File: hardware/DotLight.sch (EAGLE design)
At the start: 19 parts, among them Q1 BSH103, Q2 BSH103

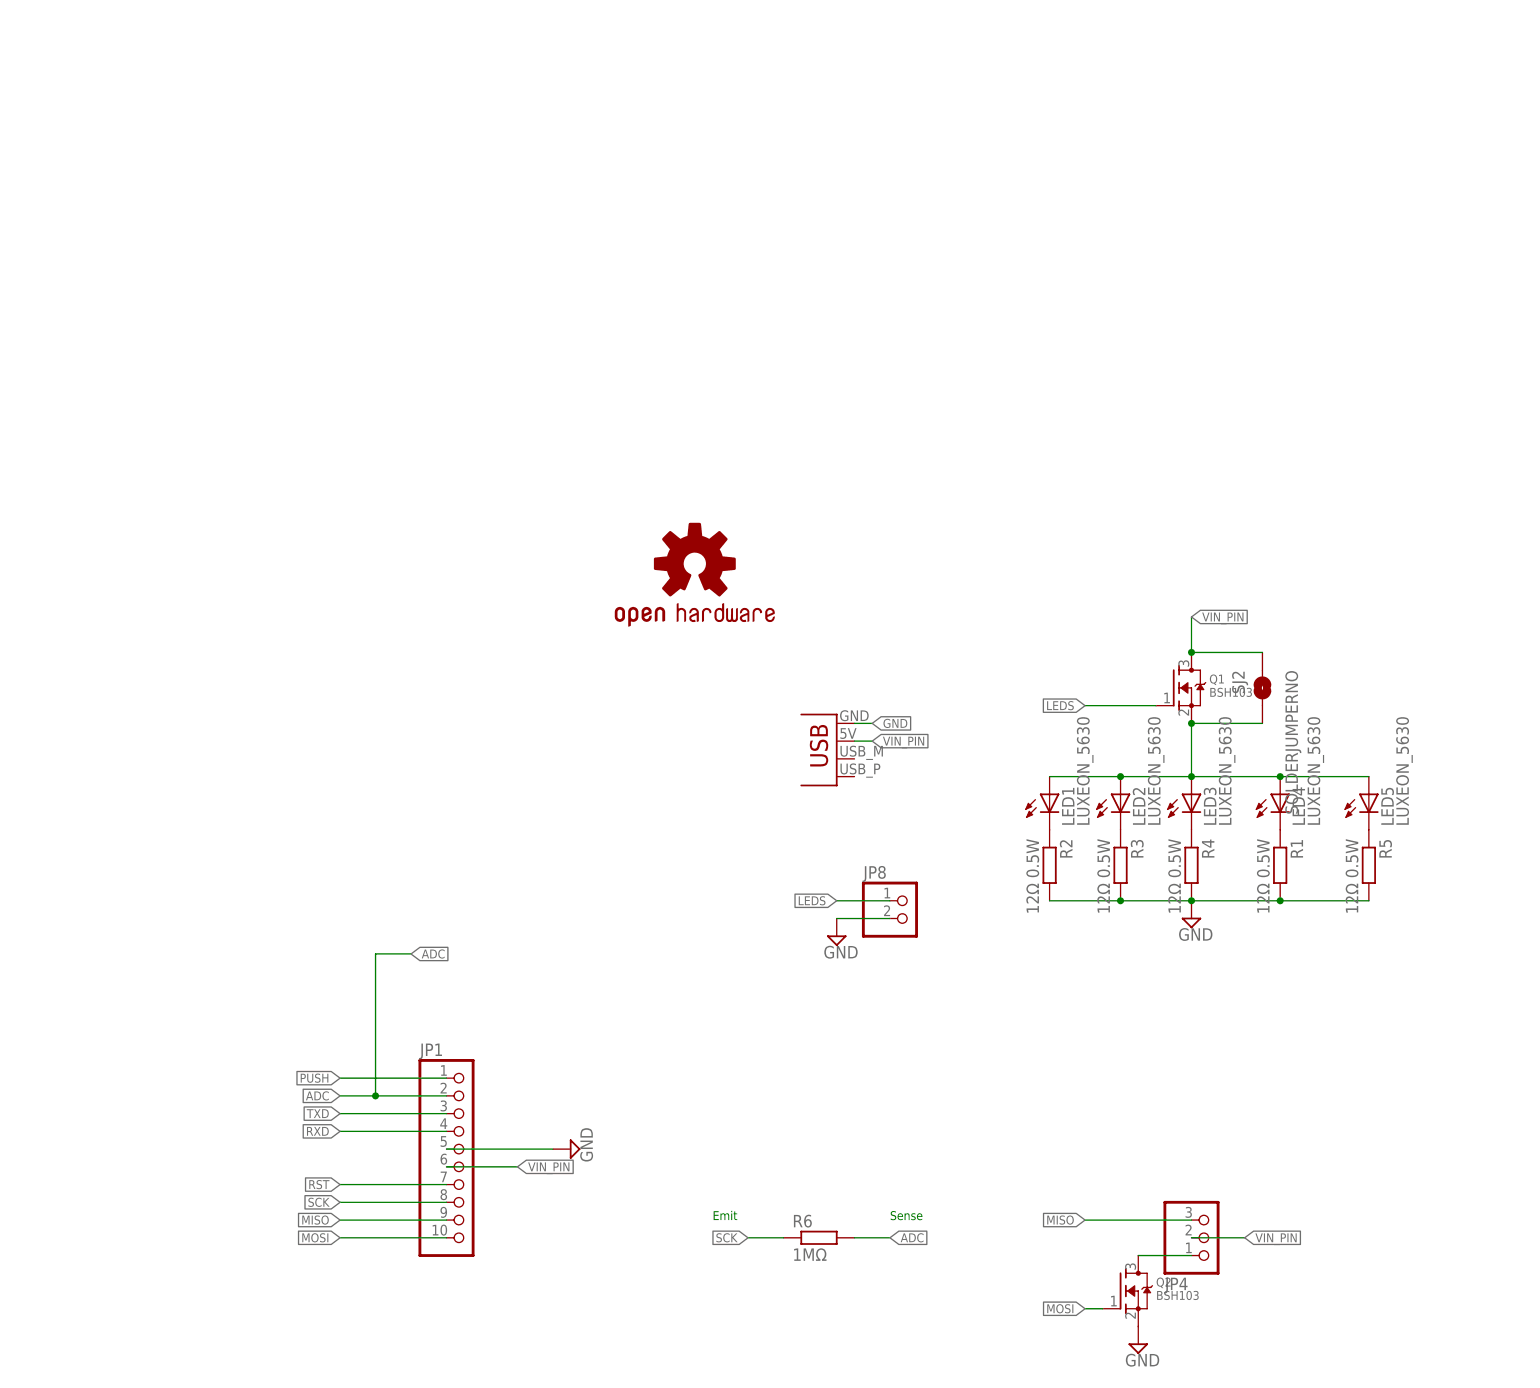
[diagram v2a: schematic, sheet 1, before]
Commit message: Add Attiny85 and usage logos
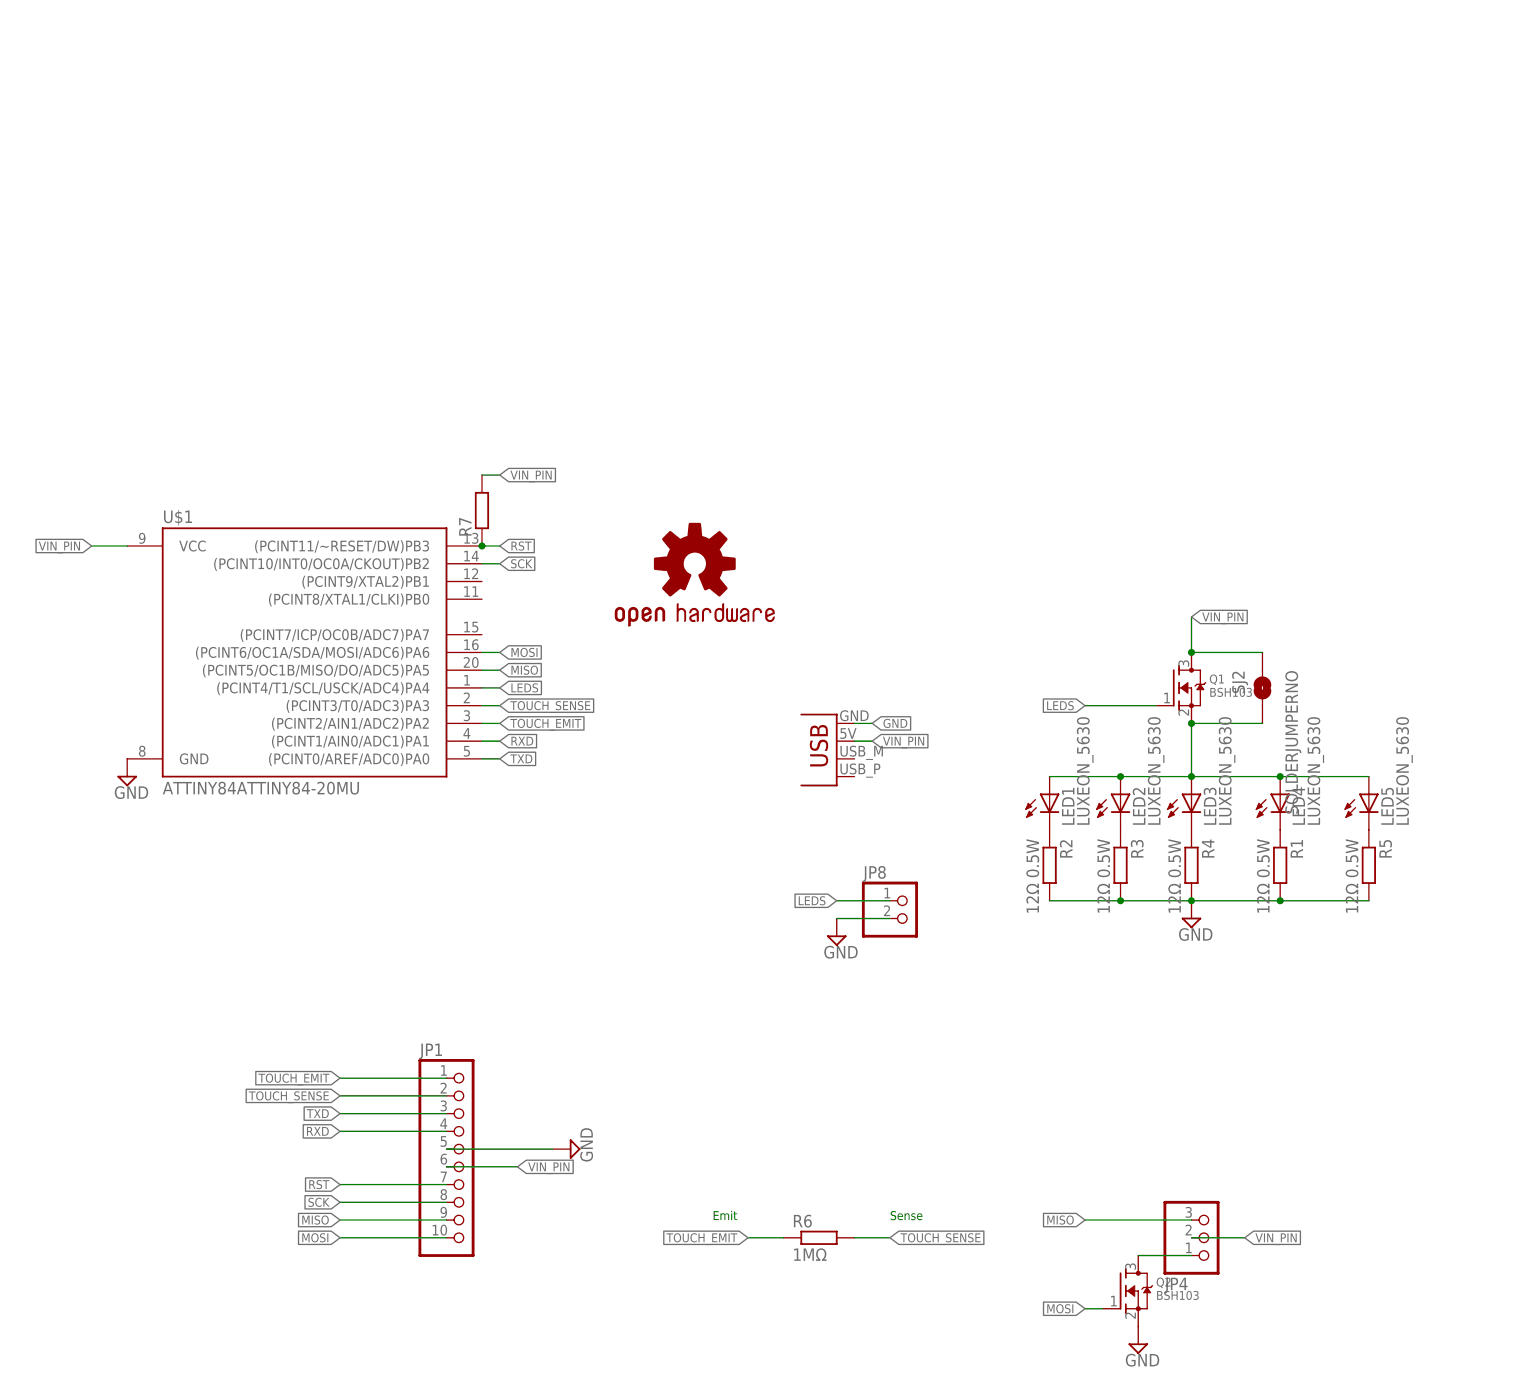
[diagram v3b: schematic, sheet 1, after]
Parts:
- added R7: (no value), rcl:R-EU_R0603
- added U$1: ATTINY84ATTINY84-20MU, SparkFun-IC-Microcontroller:ATTINY84ATTINY84-20MU
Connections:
- removed net ADC: JP1.2, R6.2
- removed net PUSH: JP1.1
- new net TOUCH_EMIT: JP1.1, R6.1, U$1.(PCINT2/AIN1/ADC2)PA2
- new net TOUCH_SENSE: JP1.2, R6.2, U$1.(PCINT3/T0/ADC3)PA3
- net GND: now also U$1.GND
- net LEDS: now also U$1.(PCINT4/T1/SCL/USCK/ADC4)PA4
- net MISO: now also U$1.(PCINT5/OC1B/MISO/DO/ADC5)PA5
- net MOSI: now also U$1.(PCINT6/OC1A/SDA/MOSI/ADC6)PA6
- net RST: now also R7.1, U$1.(PCINT11/~RESET/DW)PB3
- net RXD: now also U$1.(PCINT1/AIN0/ADC1)PA1
- net SCK: now also U$1.(PCINT10/INT0/OC0A/CKOUT)PB2; no longer R6.1
- net TXD: now also U$1.(PCINT0/AREF/ADC0)PA0
- net VIN_PIN: now also R7.2, U$1.VCC
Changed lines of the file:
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@@
 <part name="R6" library="resistor" deviceset="R-EU_" device="R1206" value="1MΩ"/>
 <part name="SJ2" library="SparkFun-Retired" deviceset="SOLDERJUMPER" device="NO"/>
+<part name="U$1" library="SparkFun-IC-Microcontroller" deviceset="ATTINY84" device="ATTINY84-20MU"/>
+<part name="SUPPLY2" library="supply2" deviceset="GND" device=""/>
+<part name="R7" library="rcl" deviceset="R-EU_" device="R0603"/>
 </parts>
 <sheets>
@@
 <instance part="R6" gate="G$1" x="129.54" y="121.92"/>
 <instance part="SJ2" gate="1" x="193.04" y="200.66" rot="MR270"/>
+<instance part="U$1" gate="G$1" x="55.88" y="205.74"/>
+<instance part="SUPPLY2" gate="GND" x="30.48" y="187.96"/>
+<instance part="R7" gate="G$1" x="81.28" y="226.06" rot="R90"/>
 </instances>
 <busses>
@@
 <pinref part="SUPPLY4" gate="GND" pin="GND"/>
 </segment>
+<segment>
+<pinref part="U$1" gate="G$1" pin="GND"/>
+<pinref part="SUPPLY2" gate="GND" pin="GND"/>
+</segment>
 </net>
 <net name="RST" class="0">
@@
 <wire x1="60.96" y1="129.54" x2="76.2" y2="129.54" width="0.1524" layer="91"/>
 </segment>
+<segment>
+<pinref part="U$1" gate="G$1" pin="(PCINT11/~RESET/DW)PB3"/>
+<wire x1="81.28" y1="220.98" x2="83.82" y2="220.98" width="0.1524" layer="91"/>
+<label x="83.82" y="220.98" size="1.27" layer="95" xref="yes"/>
+<pinref part="R7" gate="G$1" pin="1"/>
+<junction x="81.28" y="220.98"/>
+</segment>
 </net>
 <net name="MOSI" class="0">
@@
 <label x="167.64" y="111.76" size="1.27" layer="95" rot="R180" xref="yes"/>
 </segment>
+<segment>
+<pinref part="U$1" gate="G$1" pin="(PCINT6/OC1A/SDA/MOSI/ADC6)PA6"/>
+<wire x1="81.28" y1="205.74" x2="83.82" y2="205.74" width="0.1524" layer="91"/>
+<label x="83.82" y="205.74" size="1.27" layer="95" xref="yes"/>
+</segment>
 </net>
 <net name="MISO" class="0">
@@
 <label x="167.64" y="124.46" size="1.27" layer="95" rot="R180" xref="yes"/>
 </segment>
+<segment>
+<pinref part="U$1" gate="G$1" pin="(PCINT5/OC1B/MISO/DO/ADC5)PA5"/>
+<wire x1="81.28" y1="203.2" x2="83.82" y2="203.2" width="0.1524" layer="91"/>
+<label x="83.82" y="203.2" size="1.27" layer="95" xref="yes"/>
+</segment>
 </net>
 <net name="TXD" class="0">
@@
 <label x="60.96" y="139.7" size="1.27" layer="95" rot="R180" xref="yes"/>
 </segment>
+<segment>
+<pinref part="U$1" gate="G$1" pin="(PCINT0/AREF/ADC0)PA0"/>
+<wire x1="81.28" y1="190.5" x2="83.82" y2="190.5" width="0.1524" layer="91"/>
+<label x="83.82" y="190.5" size="1.27" layer="95" xref="yes"/>
+</segment>
 </net>
 <net name="SCK" class="0">
@@
 </segment>
 <segment>
-<pinref part="R6" gate="G$1" pin="1"/>
-<wire x1="124.46" y1="121.92" x2="119.38" y2="121.92" width="0.1524" layer="91"/>
-<label x="119.38" y="121.92" size="1.27" layer="95" rot="R180" xref="yes"/>
-</segment>
-</net>
-<net name="PUSH" class="0">
-<segment>
-<pinref part="JP1" gate="A" pin="1"/>
-<wire x1="76.2" y1="144.78" x2="60.96" y2="144.78" width="0.1524" layer="91"/>
-<label x="60.96" y="144.78" size="1.27" layer="95" rot="R180" xref="yes"/>
+<pinref part="U$1" gate="G$1" pin="(PCINT10/INT0/OC0A/CKOUT)PB2"/>
+<wire x1="81.28" y1="218.44" x2="83.82" y2="218.44" width="0.1524" layer="91"/>
+<label x="83.82" y="218.44" size="1.27" layer="95" xref="yes"/>
 </segment>
 </net>
@@
 <wire x1="76.2" y1="137.16" x2="60.96" y2="137.16" width="0.1524" layer="91"/>
 <label x="60.96" y="137.16" size="1.27" layer="95" rot="R180" xref="yes"/>
+</segment>
+<segment>
+<pinref part="U$1" gate="G$1" pin="(PCINT1/AIN0/ADC1)PA1"/>
+<wire x1="81.28" y1="193.04" x2="83.82" y2="193.04" width="0.1524" layer="91"/>
+<label x="83.82" y="193.04" size="1.27" layer="95" xref="yes"/>
 </segment>
 </net>
@@
 <junction x="182.88" y="205.74"/>
 </segment>
-</net>
-<net name="ADC" class="0">
-<segment>
-<wire x1="66.04" y1="162.56" x2="71.12" y2="162.56" width="0.1524" layer="91"/>
-<label x="71.12" y="162.56" size="1.27" layer="95" xref="yes"/>
-<pinref part="JP1" gate="A" pin="2"/>
-<wire x1="76.2" y1="142.24" x2="66.04" y2="142.24" width="0.1524" layer="91"/>
-<label x="60.96" y="142.24" size="1.27" layer="95" rot="R180" xref="yes"/>
-<wire x1="66.04" y1="142.24" x2="60.96" y2="142.24" width="0.1524" layer="91"/>
-<junction x="66.04" y="142.24"/>
-<wire x1="66.04" y1="162.56" x2="66.04" y2="142.24" width="0.1524" layer="91"/>
-</segment>
-<segment>
-<pinref part="R6" gate="G$1" pin="2"/>
-<wire x1="134.62" y1="121.92" x2="139.7" y2="121.92" width="0.1524" layer="91"/>
-<label x="139.7" y="121.92" size="1.27" layer="95" xref="yes"/>
+<segment>
+<pinref part="U$1" gate="G$1" pin="VCC"/>
+<wire x1="30.48" y1="220.98" x2="25.4" y2="220.98" width="0.1524" layer="91"/>
+<label x="25.4" y="220.98" size="1.27" layer="95" rot="R180" xref="yes"/>
+</segment>
+<segment>
+<pinref part="R7" gate="G$1" pin="2"/>
+<wire x1="81.28" y1="231.14" x2="83.82" y2="231.14" width="0.1524" layer="91"/>
+<label x="83.82" y="231.14" size="1.27" layer="95" xref="yes"/>
 </segment>
 </net>
@@
 <wire x1="139.7" y1="170.18" x2="132.08" y2="170.18" width="0.1524" layer="91"/>
 <label x="132.08" y="170.18" size="1.27" layer="95" rot="R180" xref="yes"/>
+</segment>
+<segment>
+<pinref part="U$1" gate="G$1" pin="(PCINT4/T1/SCL/USCK/ADC4)PA4"/>
+<wire x1="81.28" y1="200.66" x2="83.82" y2="200.66" width="0.1524" layer="91"/>
+<label x="83.82" y="200.66" size="1.27" layer="95" xref="yes"/>
 </segment>
 </net>
@@
 <wire x1="193.04" y1="195.58" x2="182.88" y2="195.58" width="0.1524" layer="91"/>
 <junction x="182.88" y="195.58"/>
+</segment>
+</net>
+<net name="TOUCH_EMIT" class="0">
+<segment>
+<pinref part="R6" gate="G$1" pin="1"/>
+<wire x1="124.46" y1="121.92" x2="119.38" y2="121.92" width="0.1524" layer="91"/>
+<label x="119.38" y="121.92" size="1.27" layer="95" rot="R180" xref="yes"/>
+</segment>
+<segment>
+<pinref part="JP1" gate="A" pin="1"/>
+<wire x1="76.2" y1="144.78" x2="60.96" y2="144.78" width="0.1524" layer="91"/>
+<label x="60.96" y="144.78" size="1.27" layer="95" rot="R180" xref="yes"/>
+</segment>
+<segment>
+<pinref part="U$1" gate="G$1" pin="(PCINT2/AIN1/ADC2)PA2"/>
+<wire x1="81.28" y1="195.58" x2="83.82" y2="195.58" width="0.1524" layer="91"/>
+<label x="83.82" y="195.58" size="1.27" layer="95" xref="yes"/>
+</segment>
+</net>
+<net name="TOUCH_SENSE" class="0">
+<segment>
+<pinref part="R6" gate="G$1" pin="2"/>
+<wire x1="134.62" y1="121.92" x2="139.7" y2="121.92" width="0.1524" layer="91"/>
+<label x="139.7" y="121.92" size="1.27" layer="95" xref="yes"/>
+</segment>
+<segment>
+<pinref part="JP1" gate="A" pin="2"/>
+<wire x1="76.2" y1="142.24" x2="60.96" y2="142.24" width="0.1524" layer="91"/>
+<label x="60.96" y="142.24" size="1.27" layer="95" rot="R180" xref="yes"/>
+</segment>
+<segment>
+<pinref part="U$1" gate="G$1" pin="(PCINT3/T0/ADC3)PA3"/>
+<wire x1="81.28" y1="198.12" x2="83.82" y2="198.12" width="0.1524" layer="91"/>
+<label x="83.82" y="198.12" size="1.27" layer="95" xref="yes"/>
 </segment>
 </net>
@@
 </sheet>
 </sheets>
-<errors>
-</errors>
 </schematic>
 </drawing>
